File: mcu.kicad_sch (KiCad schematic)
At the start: 15 parts, among them J4 Conn_01x04, SW1 EVQP7A01P, SW2 EVQP7A01P, U2 TXB0304RUTR, U8 MX25L3233FM2I-08G, U9 ESP32-S3-WROOM-1-N16R8

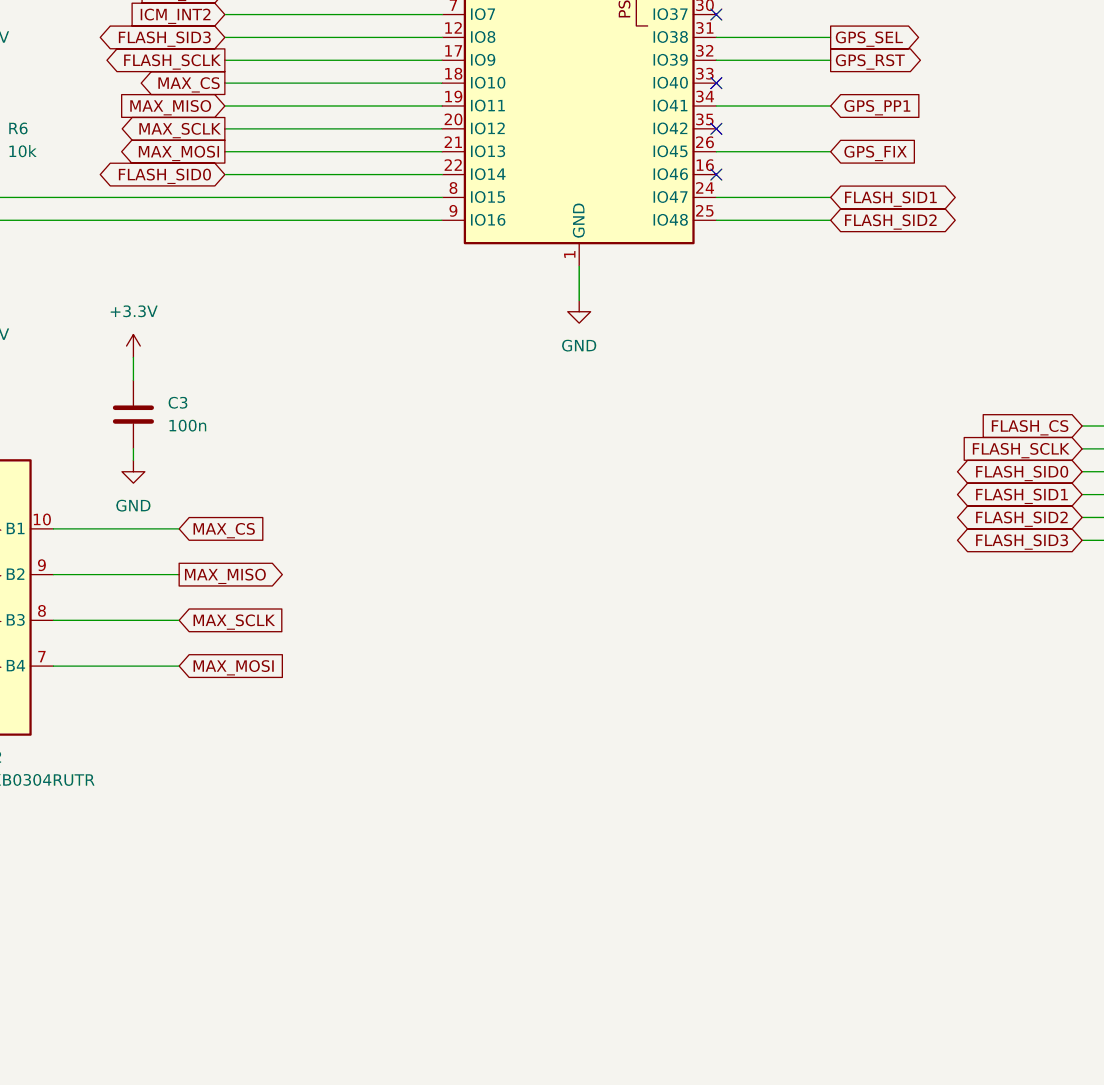
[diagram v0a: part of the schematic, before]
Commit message: Add red and IR LED for capter
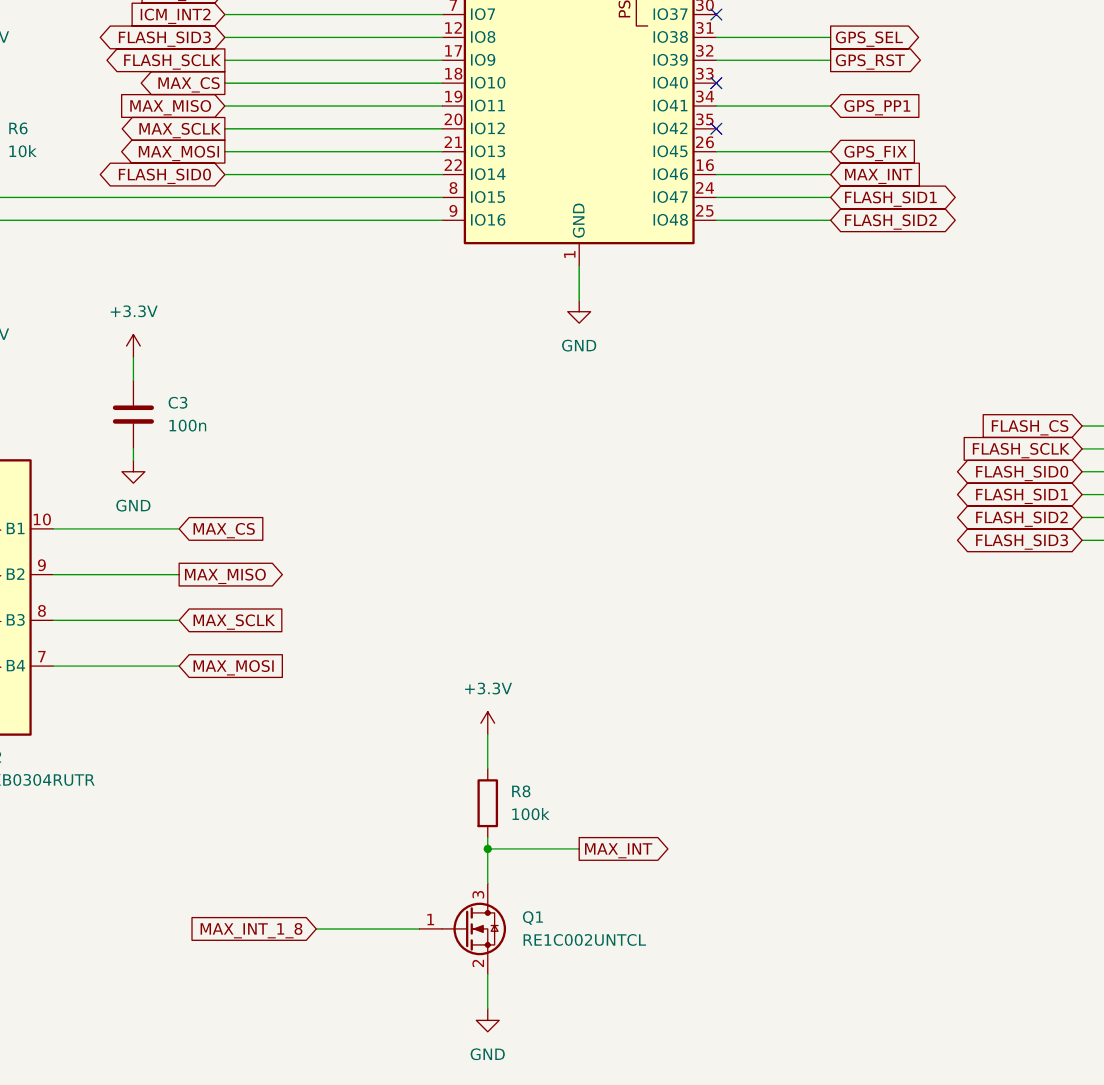
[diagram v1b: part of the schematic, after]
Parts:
- added Q1: RE1C002UNTCL, Package_TO_SOT_SMD:SOT-416, symbol Transistor_FET:Q_NMOS_GSD
- added R8: 100k, Resistor_SMD:R_0805_2012Metric, symbol Device:R
- SW2: manf# EVQ-P7A01P -> EVQP7A01P
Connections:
- net +3.3V: now also R8.1
- net GND: now also Q1.2 (S)
- net MAX_INT: now reaches U9.16 (IO46)
- net MAX_INT: now also Q1.3 (D), R8.2
- new net MAX_INT_1_8: Q1.1 (G)
- no-connect marks 6 -> 5
